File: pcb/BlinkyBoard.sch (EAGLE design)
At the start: 21 parts, among them Q1 16 MHz

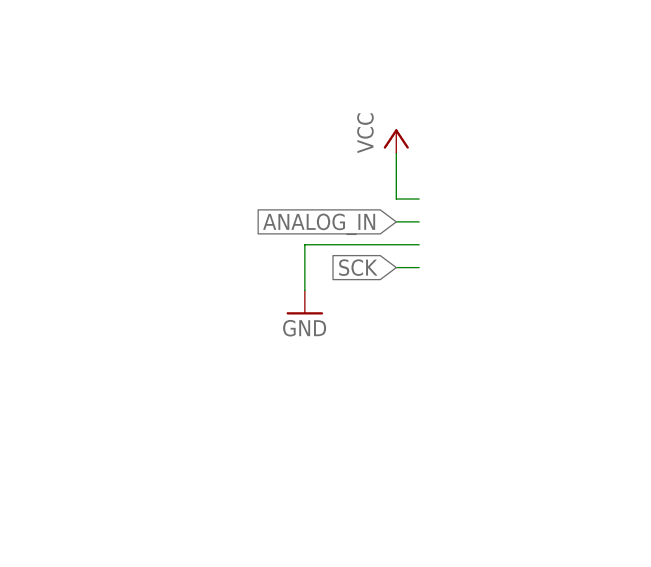
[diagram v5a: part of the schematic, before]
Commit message: Switch to thru-hole micro usb, add expansion pads on the bottom, make thermal vias on the processor smaller.
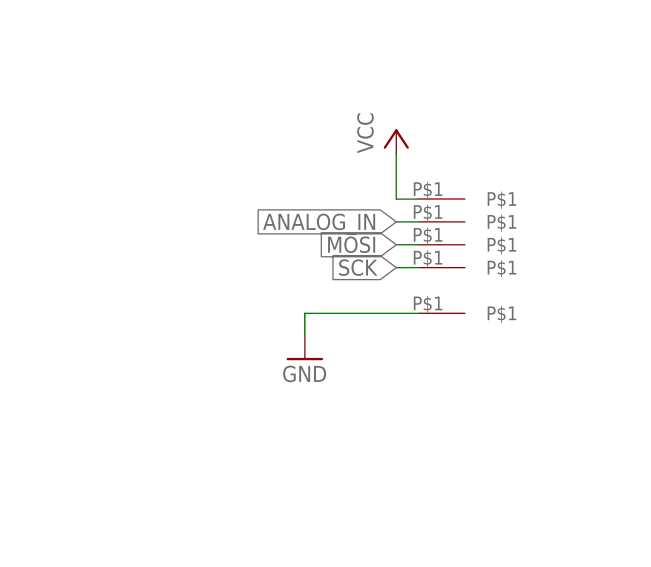
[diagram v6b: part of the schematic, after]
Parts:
- added U$10, U$11, U$12, U$13, U$14: TEST_PAD_SMT, blinkiverse:TEST_PAD_SMT
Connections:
- net ANALOG_IN: now also U$11.P$1
- net GND: now also U$13.P$1
- net MOSI: now also U$14.P$1
- net SCK: now also U$10.P$1
- net VCC: now also U$12.P$1
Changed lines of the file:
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@@
 <part name="WS3" library="blinkiverse" deviceset="WS2811_CONNECTOR" device=""/>
 <part name="P+5" library="supply1" deviceset="VCC" device=""/>
+<part name="U$10" library="blinkiverse" deviceset="TEST_PAD_SMT" device=""/>
+<part name="U$11" library="blinkiverse" deviceset="TEST_PAD_SMT" device=""/>
+<part name="U$12" library="blinkiverse" deviceset="TEST_PAD_SMT" device=""/>
+<part name="U$13" library="blinkiverse" deviceset="TEST_PAD_SMT" device=""/>
+<part name="U$14" library="blinkiverse" deviceset="TEST_PAD_SMT" device=""/>
 </parts>
 <sheets>
@@
 <instance part="P+2" gate="VCC" x="101.6" y="137.16" rot="R90"/>
 <instance part="GND1" gate="1" x="101.6" y="132.08" rot="R270"/>
-<instance part="GND2" gate="1" x="170.18" y="86.36"/>
+<instance part="GND2" gate="1" x="170.18" y="81.28"/>
 <instance part="WS3" gate="G$1" x="182.88" y="33.02"/>
 <instance part="P+5" gate="VCC" x="180.34" y="106.68"/>
+<instance part="U$10" gate="G$1" x="187.96" y="91.44"/>
+<instance part="U$11" gate="G$1" x="187.96" y="96.52"/>
+<instance part="U$12" gate="G$1" x="187.96" y="99.06"/>
+<instance part="U$13" gate="G$1" x="187.96" y="86.36"/>
+<instance part="U$14" gate="G$1" x="187.96" y="93.98"/>
 </instances>
 <busses>
@@
 <segment>
 <pinref part="GND2" gate="1" pin="GND"/>
-<wire x1="182.88" y1="93.98" x2="170.18" y2="93.98" width="0.1524" layer="91"/>
-<wire x1="170.18" y1="93.98" x2="170.18" y2="88.9" width="0.1524" layer="91"/>
+<wire x1="182.88" y1="86.36" x2="170.18" y2="86.36" width="0.1524" layer="91"/>
+<wire x1="170.18" y1="86.36" x2="170.18" y2="83.82" width="0.1524" layer="91"/>
+<pinref part="U$13" gate="G$1" pin="P$1"/>
 </segment>
 </net>
@@
 <pinref part="U$3" gate="G$1" pin="P$1"/>
 </segment>
+<segment>
+<pinref part="U$14" gate="G$1" pin="P$1"/>
+<wire x1="182.88" y1="93.98" x2="180.34" y2="93.98" width="0.1524" layer="91"/>
+<label x="180.34" y="93.98" size="1.778" layer="95" rot="R180" xref="yes"/>
+</segment>
 </net>
 <net name="MISO" class="0">
@@
 <label x="180.34" y="91.44" size="1.778" layer="95" rot="R180" xref="yes"/>
 <wire x1="180.34" y1="91.44" x2="182.88" y2="91.44" width="0.1524" layer="91"/>
+<pinref part="U$10" gate="G$1" pin="P$1"/>
 </segment>
 </net>
@@
 <label x="180.34" y="96.52" size="1.778" layer="95" rot="R180" xref="yes"/>
 <wire x1="182.88" y1="96.52" x2="180.34" y2="96.52" width="0.1524" layer="91"/>
+<pinref part="U$11" gate="G$1" pin="P$1"/>
 </segment>
 </net>
@@
 <wire x1="180.34" y1="99.06" x2="180.34" y2="104.14" width="0.1524" layer="91"/>
 <pinref part="P+5" gate="VCC" pin="VCC"/>
-</segment>
-<segment>
+<pinref part="U$12" gate="G$1" pin="P$1"/>
+</segment>
+<segment>

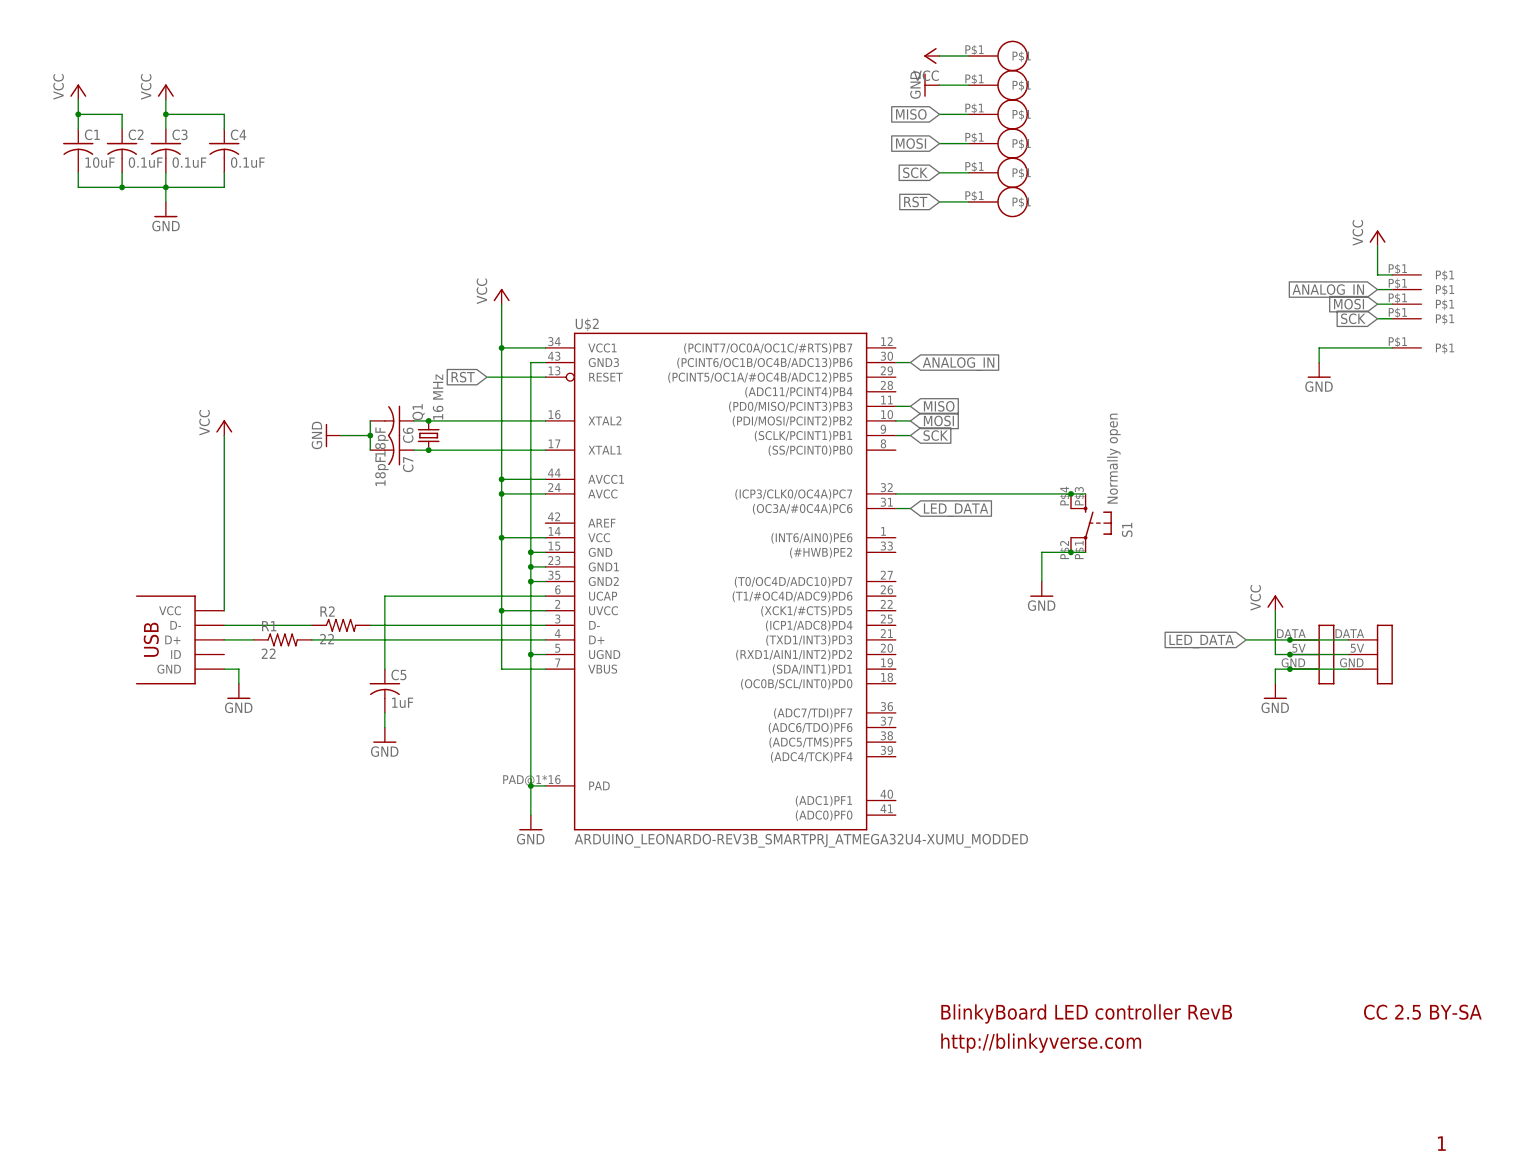
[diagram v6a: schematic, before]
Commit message: Fix thru-hole micro usb pads, switch 10uF cap to 0603 package
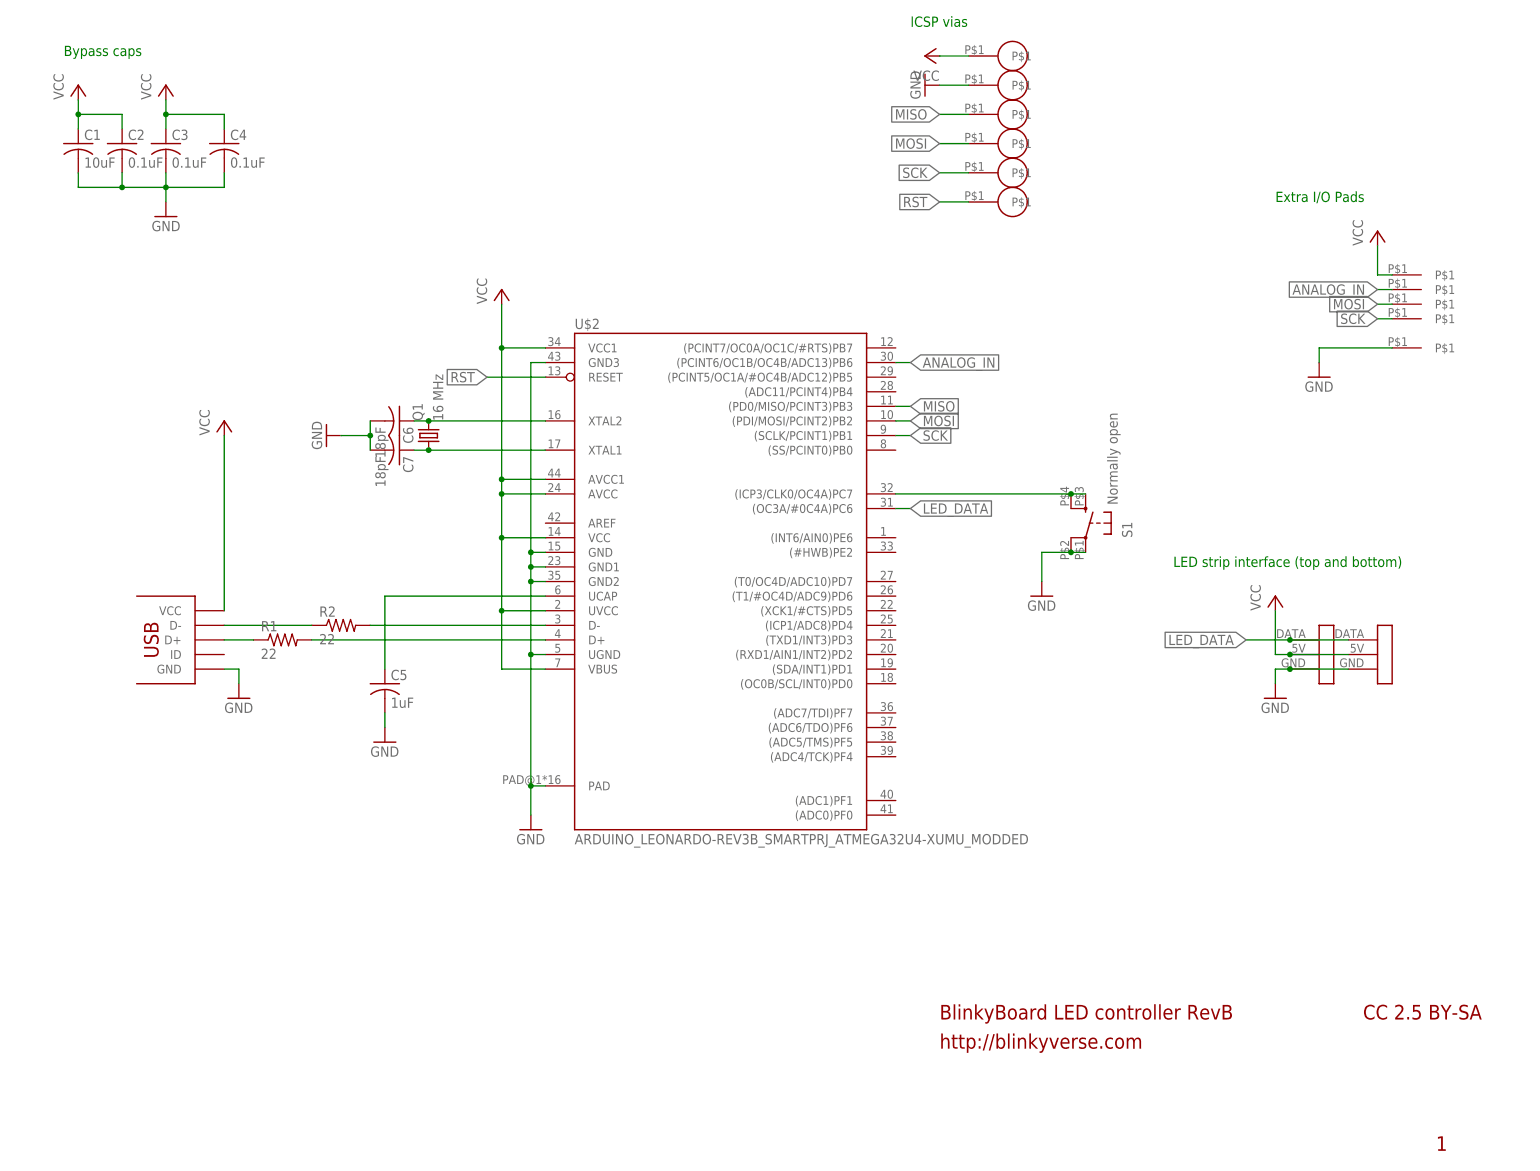
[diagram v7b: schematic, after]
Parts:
- C1: device blinkiverse:C_US -> adafruit:C-USC0603K
- U$4: value MICRO_USBSMT+DIP -> MICRO_USBSMT+THRUHULE; device blinkiverse:MICRO_USBSMT+DIP -> blinkiverse:MICRO_USBSMT+THRUHULE
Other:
- note added: "Bypass caps"
- note added: "Extra I/O Pads"
- note added: "ICSP vias"
- note added: "LED strip interface (top and bottom)"
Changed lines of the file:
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@@
 <part name="C7" library="blinkiverse" deviceset="C_US" device="" value="18pF"/>
 <part name="C2" library="blinkiverse" deviceset="C_US" device="" value="0.1uF"/>
-<part name="C1" library="blinkiverse" deviceset="C_US" device="" value="10uF"/>
+<part name="C1" library="adafruit" deviceset="C-US" device="C0603K" value="10uF"/>
 <part name="P+1" library="supply1" deviceset="VCC" device=""/>
 <part name="FRAME1" library="frames" deviceset="FRAME_A_L" device=""/>
@@
 <part name="GND4" library="supply1" deviceset="GND" device=""/>
 <part name="P+4" library="supply1" deviceset="VCC" device=""/>
-<part name="U$4" library="blinkiverse" deviceset="MICRO_USB" device="SMT+DIP"/>
+<part name="U$4" library="blinkiverse" deviceset="MICRO_USB" device="SMT+THRUHULE"/>
 <part name="GND5" library="supply1" deviceset="GND" device=""/>
 <part name="U$1" library="blinkiverse" deviceset="TEST_VIA" device=""/>
@@
 <text x="177.8" y="-30.48" size="2.54" layer="94">CC 2.5 BY-SA</text>
 <text x="190.5" y="-53.34" size="2.54" layer="94">1</text>
+<text x="-48.26" y="137.16" size="1.778" layer="91">Bypass caps</text>
+<text x="99.06" y="142.24" size="1.778" layer="91">ICSP vias</text>
+<text x="162.56" y="111.76" size="1.778" layer="91">Extra I/O Pads</text>
+<text x="144.78" y="48.26" size="1.778" layer="91">LED strip interface (top and bottom)</text>
 </plain>
 <instances>

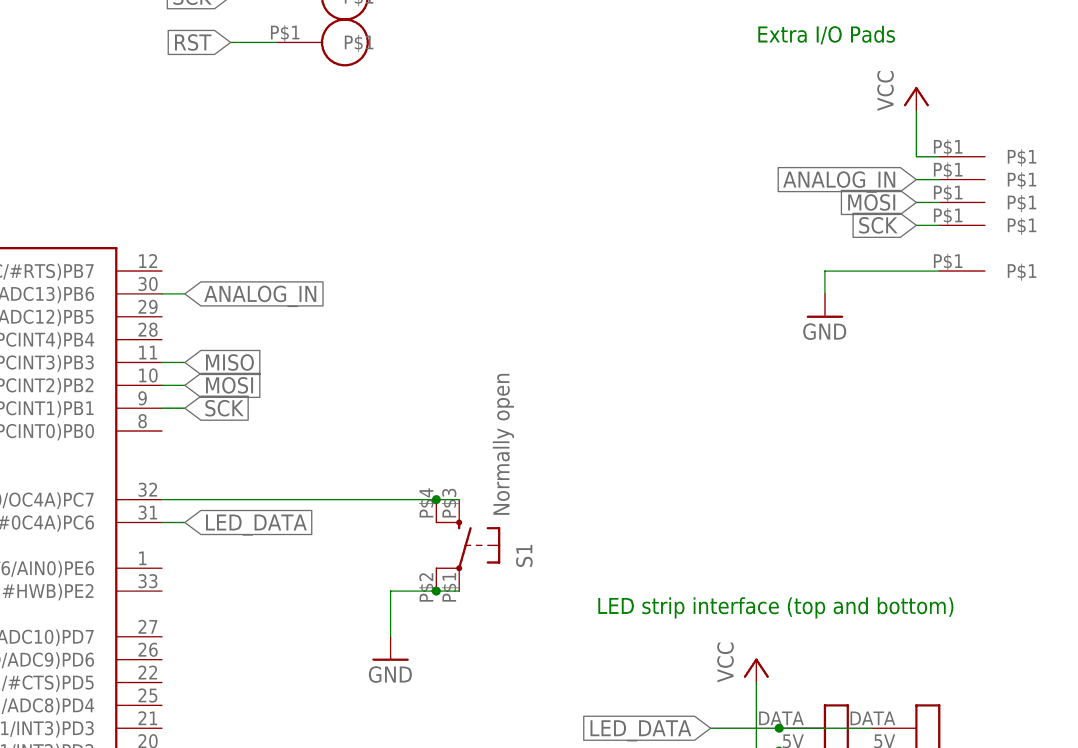
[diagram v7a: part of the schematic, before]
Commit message: Swap extra IO pads for ones that are actually Arduino pins, rename analog to A11
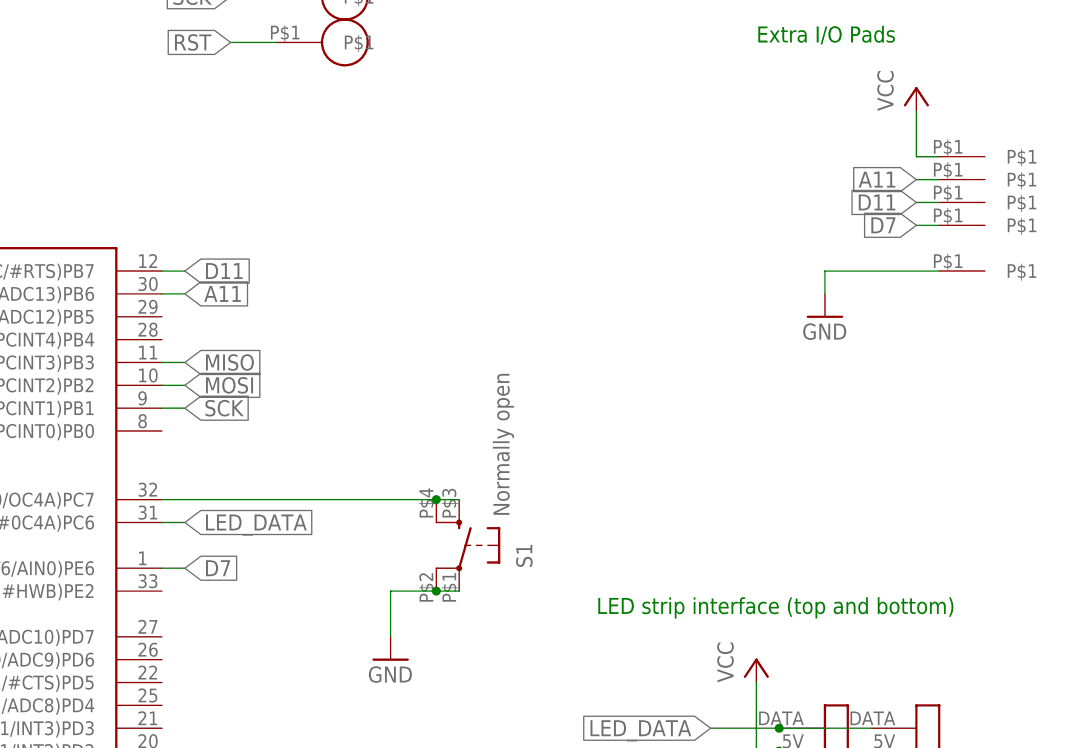
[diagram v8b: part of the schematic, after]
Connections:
- net ANALOG_IN renamed A11
- new net D11: U$14.P$1, U$2.(PCINT7/OC0A/OC1C/#RTS)PB7
- new net D7: U$10.P$1, U$2.(INT6/AIN0)PE6
- net MOSI: no longer U$14.P$1
- net SCK: no longer U$10.P$1
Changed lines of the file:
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@@
 <pinref part="U$3" gate="G$1" pin="P$1"/>
-</segment>
-<segment>
-<pinref part="U$14" gate="G$1" pin="P$1"/>
-<wire x1="182.88" y1="93.98" x2="180.34" y2="93.98" width="0.1524" layer="91"/>
-<label x="180.34" y="93.98" size="1.778" layer="95" rot="R180" xref="yes"/>
 </segment>
 </net>
@@
 <label x="104.14" y="116.84" size="1.778" layer="95" rot="R180" xref="yes"/>
 <pinref part="U$5" gate="G$1" pin="P$1"/>
-</segment>
-<segment>
-<label x="180.34" y="91.44" size="1.778" layer="95" rot="R180" xref="yes"/>
-<wire x1="180.34" y1="91.44" x2="182.88" y2="91.44" width="0.1524" layer="91"/>
-<pinref part="U$10" gate="G$1" pin="P$1"/>
 </segment>
 </net>
@@
 </segment>
 </net>
-<net name="ANALOG_IN" class="0">
+<net name="A11" class="0">
 <segment>
 <pinref part="U$2" gate="G$1" pin="(PCINT6/OC1B/OC4B/ADC13)PB6"/>
@@
 </segment>
 </net>
+<net name="D11" class="0">
+<segment>
+<pinref part="U$2" gate="G$1" pin="(PCINT7/OC0A/OC1C/#RTS)PB7"/>
+<wire x1="96.52" y1="86.36" x2="99.06" y2="86.36" width="0.1524" layer="91"/>
+<label x="99.06" y="86.36" size="1.778" layer="95" xref="yes"/>
+</segment>
+<segment>
+<pinref part="U$14" gate="G$1" pin="P$1"/>
+<wire x1="182.88" y1="93.98" x2="180.34" y2="93.98" width="0.1524" layer="91"/>
+<label x="180.34" y="93.98" size="1.778" layer="95" rot="R180" xref="yes"/>
+</segment>
+</net>
+<net name="D7" class="0">
+<segment>
+<pinref part="U$2" gate="G$1" pin="(INT6/AIN0)PE6"/>
+<wire x1="96.52" y1="53.34" x2="99.06" y2="53.34" width="0.1524" layer="91"/>
+<label x="99.06" y="53.34" size="1.778" layer="95" xref="yes"/>
+</segment>
+<segment>
+<pinref part="U$10" gate="G$1" pin="P$1"/>
+<wire x1="180.34" y1="91.44" x2="182.88" y2="91.44" width="0.1524" layer="91"/>
+<label x="180.34" y="91.44" size="1.778" layer="95" rot="R180" xref="yes"/>
+</segment>
+</net>
